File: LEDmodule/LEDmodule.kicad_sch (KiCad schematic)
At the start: 2 parts

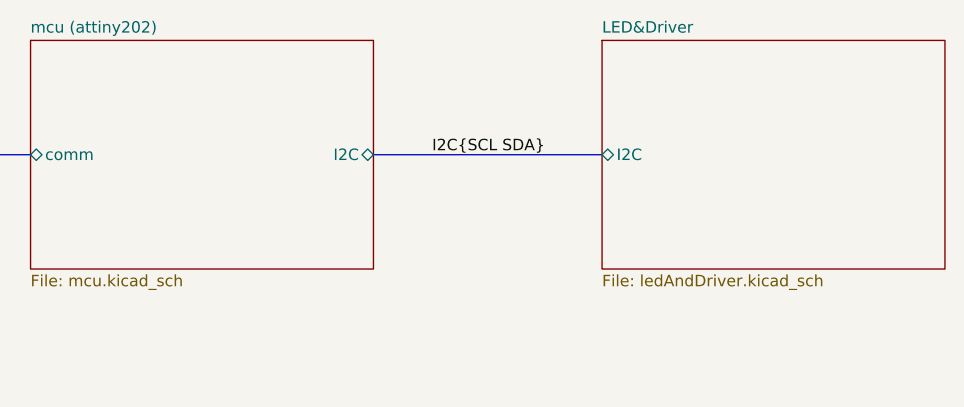
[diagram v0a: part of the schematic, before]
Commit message: Add LP5012RUK symbol
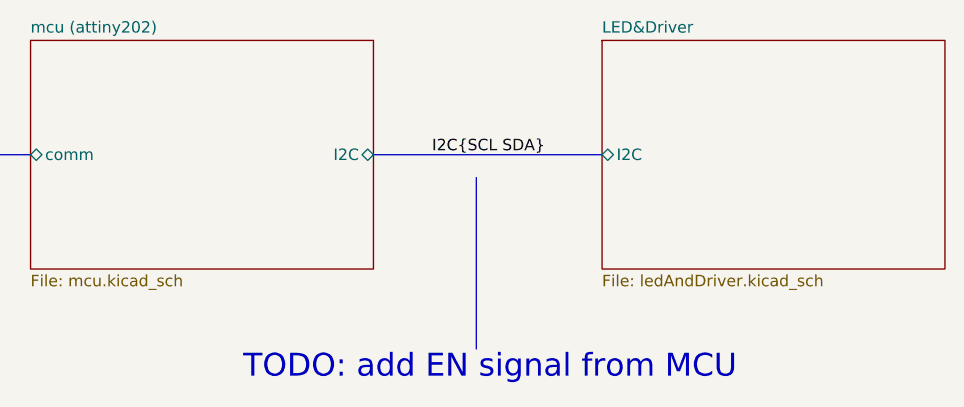
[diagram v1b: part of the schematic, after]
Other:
- note added: "TODO: add EN signal from MCU"
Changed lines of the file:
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@@
 		(comment 1 "${Designed By}")
+	)
+	(text "TODO: add EN signal from MCU"
+		(exclude_from_sim no)
+		(at 228.854 150.622 0)
+		(effects
+			(font
+				(size 2.54 2.54)
+				(color 255 0 0 1)
+			)
+		)
 	)
 	(junction
@@
 		)
 	)
+	(polyline
+		(pts
+			(xy 227.33 129.54) (xy 227.33 148.59)
+		)
+		(stroke
+			(width 0)
+			(type solid)
+			(color 255 0 0 1)
+		)
+	)

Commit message: Finalize Led&Driver
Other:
- sheet LED&Driver ports: added LP5015_EN; removed none
- sheet mcu (attiny202) ports: added LP5015_EN; removed none
- note removed: "TODO: add EN signal from MCU"
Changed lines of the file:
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@@
 		(comment 1 "${Designed By}")
-	)
-	(text "TODO: add EN signal from MCU"
-		(exclude_from_sim no)
-		(at 228.854 150.622 0)
-		(effects
-			(font
-				(size 2.54 2.54)
-				(color 255 0 0 1)
-			)
-		)
 	)
 	(junction
@@
 	(bus
 		(pts
-			(xy 215.9 127) (xy 241.3 127)
+			(xy 215.9 125.73) (xy 241.3 125.73)
 		)
 		(stroke
@@
 		)
 	)
-	(polyline
-		(pts
-			(xy 227.33 129.54) (xy 227.33 148.59)
-		)
-		(stroke
-			(width 0)
-			(type solid)
-			(color 255 0 0 1)
-		)
-	)
 	(wire
 		(pts
@@
 	(wire
 		(pts
+			(xy 215.9 129.54) (xy 241.3 129.54)
+		)
+		(stroke
+			(width 0)
+			(type default)
+		)
+	)
+	(wire
+		(pts
 			(xy 101.6 82.55) (xy 101.6 120.65)
 		)
@@
 	)
 	(label "I2C{SCL SDA}"
-		(at 234.95 127 180)
+		(at 234.95 125.73 180)
 		(effects
 			(font
@@
 		)
 		(pin "I2C" bidirectional
-			(at 215.9 127 0)
+			(at 215.9 125.73 0)
+			(effects
+				(font
+					(size 1.27 1.27)
+				)
+				(justify right)
+			)
+		)
+		(pin "LP5015_EN" output
+			(at 215.9 129.54 0)
 			(effects
 				(font
@@
 		)
 		(pin "I2C" bidirectional
-			(at 241.3 127 180)
-			(effects
-				(font
+			(at 241.3 125.73 180)
+			(effects
+				(font
+					(size 1.27 1.27)
+				)
+				(justify left)
+			)
+		)
+		(pin "LP5015_EN" input
+			(at 241.3 129.54 180)
+			(effects
+				(font

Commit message: Add start of comm's
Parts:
- removed J?: Conn_01x02_Socket, symbol Connector:Conn_01x02_Socket
- added J1: Conn_01x02_Socket, symbol Connector:Conn_01x02_Socket
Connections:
- net input protection 2/unp1: now also J1.1 (Pin_1)
- net input protection 2/unp2: now also J1.2 (Pin_2)
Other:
- sheet mcu (attiny202) renamed mcu
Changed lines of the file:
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@@
-	)
-	(junction
-		(at 101.6 120.65)
-		(diameter 0)
-		(color 0 0 0 0)
 	)
 	(junction
@@
 	)
 	(junction
-		(at 88.9 133.35)
+		(at 88.9 128.27)
 		(diameter 0)
 		(color 0 0 0 0)
 	)
+	(junction
+		(at 101.6 115.57)
+		(diameter 0)
+		(color 0 0 0 0)
+	)
 	(wire
 		(pts
@@
 	(wire
 		(pts
-			(xy 25.4 125.73) (xy 31.75 125.73)
+			(xy 101.6 115.57) (xy 101.6 120.65)
 		)
 		(stroke
@@
 	(wire
 		(pts
-			(xy 31.75 125.73) (xy 31.75 121.92)
+			(xy 76.2 115.57) (xy 101.6 115.57)
 		)
 		(stroke
@@
 	(wire
 		(pts
-			(xy 31.75 121.92) (xy 38.1 121.92)
+			(xy 25.4 120.65) (xy 31.75 120.65)
 		)
 		(stroke
@@
 	(wire
 		(pts
+			(xy 88.9 128.27) (xy 88.9 133.35)
+		)
+		(stroke
+			(width 0)
+			(type default)
+		)
+	)
+	(wire
+		(pts
 			(xy 88.9 44.45) (xy 88.9 95.25)
 		)
@@
 	(wire
 		(pts
-			(xy 88.9 133.35) (xy 76.2 133.35)
+			(xy 31.75 115.57) (xy 31.75 120.65)
+		)
+		(stroke
+			(width 0)
+			(type default)
+		)
+	)
+	(wire
+		(pts
+			(xy 31.75 115.57) (xy 38.1 115.57)
 		)
 		(stroke
@@
 	(wire
 		(pts
-			(xy 76.2 120.65) (xy 101.6 120.65)
-		)
-		(stroke
-			(width 0)
-			(type default)
-		)
-	)
-	(wire
-		(pts
 			(xy 31.75 90.17) (xy 31.75 95.25)
 		)
@@
 	(wire
 		(pts
-			(xy 101.6 82.55) (xy 101.6 120.65)
+			(xy 101.6 82.55) (xy 101.6 115.57)
+		)
+		(stroke
+			(width 0)
+			(type default)
+		)
+	)
+	(wire
+		(pts
+			(xy 25.4 123.19) (xy 31.75 123.19)
 		)
 		(stroke
@@
 	(wire
 		(pts
-			(xy 31.75 133.35) (xy 38.1 133.35)
-		)
-		(stroke
-			(width 0)
-			(type default)
-		)
-	)
-	(wire
-		(pts
-			(xy 31.75 128.27) (xy 31.75 133.35)
-		)
-		(stroke
-			(width 0)
-			(type default)
-		)
-	)
-	(wire
-		(pts
-			(xy 88.9 95.25) (xy 88.9 133.35)
-		)
-		(stroke
-			(width 0)
-			(type default)
-		)
-	)
-	(wire
-		(pts
-			(xy 25.4 128.27) (xy 31.75 128.27)
+			(xy 31.75 128.27) (xy 38.1 128.27)
+		)
+		(stroke
+			(width 0)
+			(type default)
+		)
+	)
+	(wire
+		(pts
+			(xy 31.75 123.19) (xy 31.75 128.27)
+		)
+		(stroke
+			(width 0)
+			(type default)
+		)
+	)
+	(wire
+		(pts
+			(xy 76.2 128.27) (xy 88.9 128.27)
+		)
+		(stroke
+			(width 0)
+			(type default)
+		)
+	)
+	(wire
+		(pts
+			(xy 88.9 95.25) (xy 88.9 128.27)
 		)
 		(stroke
@@
 	(symbol
 		(lib_id "Connector:Conn_01x02_Socket")
-		(at 20.32 125.73 0)
+		(at 20.32 120.65 0)
 		(mirror y)
 		(unit 1)
@@
 		(dnp no)
 		(fields_autoplaced yes)
-		(property "Reference" "J?"
-			(at 20.955 120.65 0)
+		(property "Reference" "J1"
+			(at 20.955 115.57 0)
 			(effects
 				(font
@@
 		)
 		(property "Value" "Conn_01x02_Socket"
-			(at 20.955 123.19 0)
+			(at 20.955 118.11 0)
 			(effects
 				(font
@@
 		)
 		(property "Footprint" ""
-			(at 20.32 125.73 0)
+			(at 20.32 120.65 0)
 			(effects
 				(font
@@
 		)
 		(property "Datasheet" "~"
-			(at 20.32 125.73 0)
+			(at 20.32 120.65 0)
 			(effects
 				(font
@@
 		)
 		(property "Description" "Generic connector, single row, 01x02, script generated"
-			(at 20.32 125.73 0)
+			(at 20.32 120.65 0)
 			(effects
 				(font
@@
 			)
 		)
+		(pin "1"
+		)
 		(pin "2"
-		)
-		(pin "1"
-		)
-		(instances
-			(project ""
-				(path "/80a08b48-2579-42cd-b65f-533f20aa7c1b"
-					(reference "J?")
-					(unit 1)
-				)
-			)
-		)
-	)
-	(sheet
-		(at 38.1 114.3)
-		(size 38.1 25.4)
-		(exclude_from_sim no)
-		(in_bom yes)
-		(on_board yes)
-		(dnp no)
-		(fields_autoplaced yes)
-		(stroke
-			(width 0.1524)
-			(type solid)
-		)
-		(fill
-			(color 0 0 0 0.0000)
-		)
-		(property "Sheetname" "input protection 2"
-			(at 38.1 113.5884 0)
-			(effects
-				(font
-					(size 1.27 1.27)
-				)
-				(justify left bottom)
-			)
-		)
-		(property "Sheetfile" "inputProtection.kicad_sch"
-			(at 38.1 140.2846 0)
-			(effects
-				(font
-					(size 1.27 1.27)
-				)
-				(justify left top)
-			)
-		)
-		(pin "prot1" bidirectional
-			(at 76.2 120.65 0)
-			(effects
-				(font
-					(size 1.27 1.27)
-				)
-				(justify right)
-			)
-		)
-		(pin "prot2" bidirectional
-			(at 76.2 133.35 0)
-			(effects
-				(font
-					(size 1.27 1.27)
-				)
-				(justify right)
-			)
-		)
-		(pin "unp1" bidirectional
-			(at 38.1 121.92 180)
-			(effects
-				(font
-					(size 1.27 1.27)
-				)
-				(justify left)
-			)
-		)
-		(pin "unp2" bidirectional
-			(at 38.1 133.35 180)
-			(effects
-				(font
-					(size 1.27 1.27)
-				)
-				(justify left)
-			)
 		)
 		(instances
 			(project "LEDmodule"
 				(path "/80a08b48-2579-42cd-b65f-533f20aa7c1b"
-					(page "7")
+					(reference "J1")
+					(unit 1)
 				)
 			)
@@
 			(color 0 0 0 0.0000)
 		)
-		(property "Sheetname" "mcu (attiny202)"
+		(property "Sheetname" "mcu"
 			(at 177.8 113.5884 0)
 			(effects
@@
 				)
 			)
+		)
+	)
+	(sheet
+		(at 38.1 109.22)
+		(size 38.1 25.4)
+		(exclude_from_sim no)
+		(in_bom yes)
+		(on_board yes)
+		(dnp no)
+		(fields_autoplaced yes)
+		(stroke
+			(width 0.1524)
+			(type solid)
+		)
+		(fill
+			(color 0 0 0 0.0000)
+		)
+		(property "Sheetname" "input protection 2"
+			(at 38.1 108.5084 0)
+			(effects
+				(font
+					(size 1.27 1.27)
+				)
+				(justify left bottom)
+			)
+		)
+		(property "Sheetfile" "inputProtection.kicad_sch"
+			(at 38.1 135.2046 0)
+			(effects
+				(font
+					(size 1.27 1.27)
+				)
+				(justify left top)
+			)
+		)
+		(pin "prot1" bidirectional
+			(at 76.2 115.57 0)
+			(effects
+				(font
+					(size 1.27 1.27)
+				)
+				(justify right)
+			)
+		)
+		(pin "prot2" bidirectional
+			(at 76.2 128.27 0)
+			(effects
+				(font
+					(size 1.27 1.27)
+				)
+				(justify right)
+			)
+		)
+		(pin "unp1" bidirectional
+			(at 38.1 115.57 180)
+			(effects
+				(font
+					(size 1.27 1.27)
+				)
+				(justify left)
+			)
+		)
+		(pin "unp2" bidirectional
+			(at 38.1 128.27 180)
+			(effects
+				(font
+					(size 1.27 1.27)
+				)
+				(justify left)
+			)
+		)
+		(instances
+			(project "LEDmodule"
+				(path "/80a08b48-2579-42cd-b65f-533f20aa7c1b"
+					(page "7")
+				)
+			)
